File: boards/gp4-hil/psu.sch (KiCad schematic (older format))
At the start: 0 parts

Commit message: Continued HiL test board
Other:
- note added: "Low current rails:\n* 1V25 precision reference for XADC\n\nHigh current rails (LTC3374):\n* 2V5 PHY analog\n* 1V8 FPGA VCCAUX/VCCXADC, PHY I/O\n* 1V2 PHY analog/digital core\n* 1V0 FPGA VCCINT/VCCBRAM\n\nVariable rails:\n* 7V5 Vpp\n* 0-3.4V Vdd/VCCO1\n* 0-3.4V VCCO2\n\nInput: Unregulated 5V DC"
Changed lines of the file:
@@
 LIBS:special-azonenberg
 LIBS:xilinx-azonenberg
+LIBS:conn
+LIBS:gp4-hil-cache
 EELAYER 25 0
 EELAYER END
 $Descr A4 11693 8268
 encoding utf-8
-Sheet 1 6
+Sheet 2 7
 Title "GreenPak Hardware-In-Loop Test Platform"
 Date "2016-05-09"
@@
 Comment4 ""
 $EndDescr
+Text Notes 5200 3450 0    60   ~ 0
+Low current rails:\n* 1V25 precision reference for XADC\n\nHigh current rails (LTC3374):\n* 2V5 PHY analog\n* 1V8 FPGA VCCAUX/VCCXADC, PHY I/O\n* 1V2 PHY analog/digital core\n* 1V0 FPGA VCCINT/VCCBRAM\n\nVariable rails:\n* 7V5 Vpp\n* 0-3.4V Vdd/VCCO1\n* 0-3.4V VCCO2\n\nInput: Unregulated 5V DC
 $EndSCHEMATC

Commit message: Continued work on gp4-hil board schematic
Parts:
- added U3: LTC3374-QFN, symbol LTC3374-QFN
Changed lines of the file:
@@
 Sheet 2 7
 Title "GreenPak Hardware-In-Loop Test Platform"
-Date "2016-05-09"
+Date "2016-05-10"
 Rev "0.1"
 Comp "Andrew Zonenberg"
@@
 Text Notes 5200 3450 0    60   ~ 0
 Low current rails:\n* 1V25 precision reference for XADC\n\nHigh current rails (LTC3374):\n* 2V5 PHY analog\n* 1V8 FPGA VCCAUX/VCCXADC, PHY I/O\n* 1V2 PHY analog/digital core\n* 1V0 FPGA VCCINT/VCCBRAM\n\nVariable rails:\n* 7V5 Vpp\n* 0-3.4V Vdd/VCCO1\n* 0-3.4V VCCO2\n\nInput: Unregulated 5V DC
+$Comp
+L LTC3374-QFN U3
+U 1 1 5732D550
+P 2550 4200
+F 0 "U3" H 3477 4511 60  0000 L CNN
+F 1 "LTC3374-QFN" H 3477 4405 60  0000 L CNN
+F 2 "" H 2550 4200 60  0000 C CNN
+F 3 "" H 2550 4200 60  0000 C CNN
+	1    2550 4200
+	1    0    0    -1
+$EndComp
+Text HLabel 8000 4650 0    60   Output ~ 0
+DUT_VPP
+Text HLabel 8000 4000 0    60   Output ~ 0
+2V5
+Text HLabel 8000 4100 0    60   Output ~ 0
+1V8
+Text HLabel 8000 4200 0    60   Output ~ 0
+1V2
+Text HLabel 8000 4300 0    60   Output ~ 0
+1V0
+Text HLabel 8000 5150 0    60   Output ~ 0
+GND
+Text HLabel 8000 4750 0    60   Output ~ 0
+DUT_VDD1
+Text HLabel 8000 4850 0    60   Output ~ 0
+DUT_VDD2
 $EndSCHEMATC

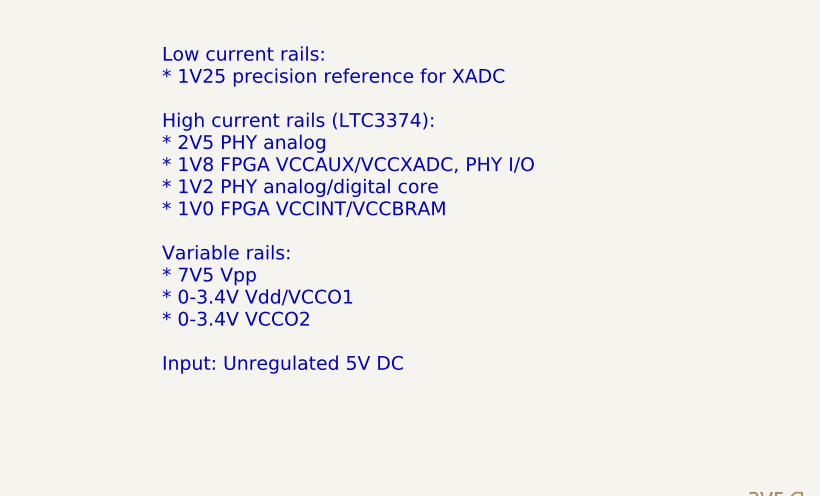
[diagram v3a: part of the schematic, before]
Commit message: Continued analog input schematic
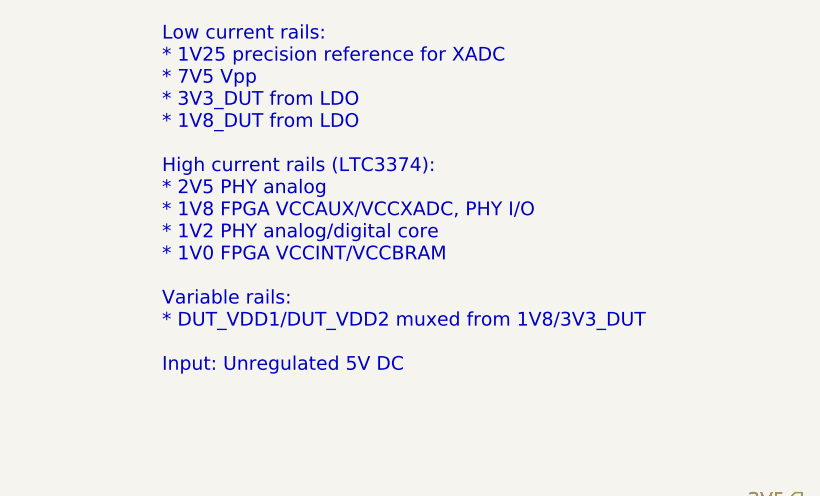
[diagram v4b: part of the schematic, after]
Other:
- note added: "Low current rails:\n* 1V25 precision reference for XADC\n* 7V5 Vpp\n* 3V3_DUT from LDO\n* 1V8_DUT from LDO\n\nHigh current rails (LTC3374):\n* 2V5 PHY analog\n* 1V8 FPGA VCCAUX/VCCXADC, PHY I/O\n* 1V2 PHY analog/digital core\n* 1V0 FPGA VCCINT/VCCBRAM\n\nVariable rails:\n* DUT_VDD1/DUT_VDD2 muxed from 1V8/3V3_DUT\n\nInput: Unregulated 5V DC"
- note removed: "Low current rails:\n* 1V25 precision reference for XADC\n\nHigh current rails (LTC3374):\n* 2V5 PHY analog\n* 1V8 FPGA VCCAUX/VCCXADC, PHY I/O\n* 1V2 PHY analog/digital core\n* 1V0 FPGA VCCINT/VCCBRAM\n\nVariable rails:\n* 7V5 Vpp\n* 0-3.4V Vdd/VCCO1\n* 0-3.4V VCCO2\n\nInput: Unregulated 5V DC"
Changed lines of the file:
@@
 $EndDescr
 Text Notes 5200 3450 0    60   ~ 0
-Low current rails:\n* 1V25 precision reference for XADC\n\nHigh current rails (LTC3374):\n* 2V5 PHY analog\n* 1V8 FPGA VCCAUX/VCCXADC, PHY I/O\n* 1V2 PHY analog/digital core\n* 1V0 FPGA VCCINT/VCCBRAM\n\nVariable rails:\n* 7V5 Vpp\n* 0-3.4V Vdd/VCCO1\n* 0-3.4V VCCO2\n\nInput: Unregulated 5V DC
+Low current rails:\n* 1V25 precision reference for XADC\n* 7V5 Vpp\n* 3V3_DUT from LDO\n* 1V8_DUT from LDO\n\nHigh current rails (LTC3374):\n* 2V5 PHY analog\n* 1V8 FPGA VCCAUX/VCCXADC, PHY I/O\n* 1V2 PHY analog/digital core\n* 1V0 FPGA VCCINT/VCCBRAM\n\nVariable rails:\n* DUT_VDD1/DUT_VDD2 muxed from 1V8/3V3_DUT\n\nInput: Unregulated 5V DC
 $Comp
 L LTC3374-QFN U3

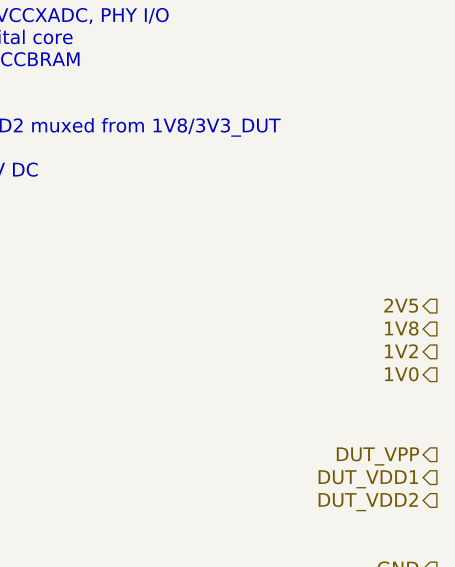
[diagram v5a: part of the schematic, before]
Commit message: Added DACs, minor page layout tweaks, lots of decoupling
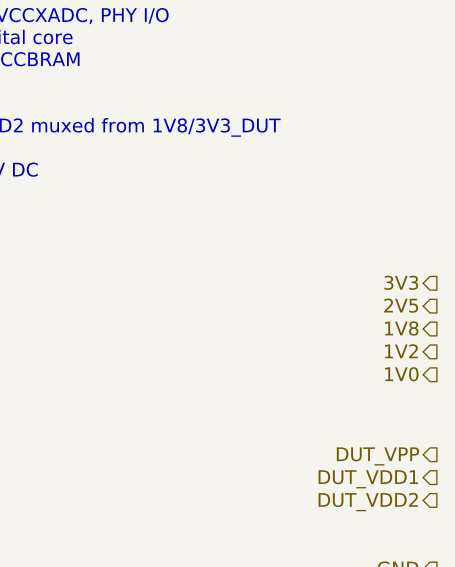
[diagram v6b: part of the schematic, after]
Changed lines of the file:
@@
 EELAYER 25 0
 EELAYER END
-$Descr A4 11693 8268
+$Descr A2 23386 16535
 encoding utf-8
 Sheet 2 7
 Title "GreenPak Hardware-In-Loop Test Platform"
-Date "2016-05-12"
+Date "2016-05-13"
 Rev "0.1"
 Comp "Andrew Zonenberg"
-Comment1 ""
+Comment1 "Power regulation"
 Comment2 ""
 Comment3 ""
@@
 Text HLabel 8000 4850 0    60   Output ~ 0
 DUT_VDD2
+Text HLabel 8000 3900 0    60   Output ~ 0
+3V3
 $EndSCHEMATC

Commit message: Schematic entry for 1V0 PSU
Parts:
- added C116, C117, C118, C119, C120, C121, C123, C124: 22 uF, symbol C
- added C122: 100 uF, symbol C
- added K1: CONN_3_PWROUT, symbol CONN_3_PWROUT
- added L6: 2.2 uH 8.2A, symbol INDUCTOR_PWROUT
- added R100: 1K, symbol R
- added R101: 2.55K, symbol R
- added R102: 10.2K, symbol R
- added R103: 0, symbol R
- added unit 1 of U3
- added unit 3 of U3
- added unit 4 of U3
- added unit 5 of U3
- added unit 6 of U3
- added unit 7 of U3
- added unit 8 of U3
- added unit 9 of U3
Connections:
- net 1V0: now also C122.1, L6.1, R103.1
- net 2V5: now also R100.2
- net GND: now also U3.37 (EN2), C116.2, C117.2, C118.2, C119.2, C120.2, C121.2, C122.2, C123.2, C124.2, K1.2 (PM), R102.1, U3.13 (EN4), U3.14 (EN3), U3.16 (SYNC), U3.PAD (GND)
- new net 1V0_VSENSE: R101.1, R103.2
- new net 5V0: C116.1, C117.1, C118.1, C119.1, C120.1, C121.1, C123.1, C124.1, U3.11 (VIN4), U3.12 (FB4), U3.17 (RT), U3.2 (VIN1), U3.34 (MODE), U3.35 (VCC), U3.38 (EN1), U3.5 (VIN2), U3.6 (FB2), U3.7 (FB3), U3.8 (VIN3)
- new net 5V0_IN: K1.1 (P1)
- new net FB_1V0: R101.2, R102.2, U3.1 (FB1)
- new net PSU_PGOOD: R100.1, U3.15 (PGOOD_ALL)
- new net PSU_VTEMP: U3.36 (TEMP)
- new net SW_1V0: L6.2, U3.10 (SW4), U3.3 (SW1), U3.4 (SW2), U3.9 (SW3)
- no-connect marks 0 -> 1
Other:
- note added: "1V0 input caps"
- note added: "Low current rails:\n* 1V25 precision reference for XADC\n* 7V5 Vpp\n\nHigh current rails (LTC3374):\n* 3V3 DUT\n* 2V5 PHY analog\n* 1V8 FPGA VCCAUX/VCCXADC, PHY I/O, DUT\n* 1V2 PHY analog/digital core\n* 1V0 FPGA VCCINT/VCCBRAM\n\nVariable rails:\n* DUT_VDD1/DUT_VDD2 muxed from 1V8/3V3\n\nInput: Unregulated 5V DC"
- note added: "Power inlet"
- note added: "TODO: Load switching for DUT_VDDx\nTODO: Load switching for VPP"
- note added: "TODO: See if we can get low enough power to run off USB?"
- note added: "TODO: VCC cap"
- note added: "TODO: what rail to pull to?"
- note added: "Target loads:\n* 3V3 @ 1A\n* 2V5 @ 1A\n* 1V8 @ 1A\n* 1V2 @ 1A\n* 1V0 @ 4A\n\nFPGA:\n* 1V0 @ 1.25A\n* 1V8 @ 0.1A\n\nPHY:\n* 2V5 @ 0.1 A\n* 1V8 @ 0.1A\n* 1V2 @ 0.25 A"
- note removed: "Low current rails:\n* 1V25 precision reference for XADC\n* 7V5 Vpp\n* 3V3_DUT from LDO\n* 1V8_DUT from LDO\n\nHigh current rails (LTC3374):\n* 2V5 PHY analog\n* 1V8 FPGA VCCAUX/VCCXADC, PHY I/O\n* 1V2 PHY analog/digital core\n* 1V0 FPGA VCCINT/VCCBRAM\n\nVariable rails:\n* DUT_VDD1/DUT_VDD2 muxed from 1V8/3V3_DUT\n\nInput: Unregulated 5V DC"
